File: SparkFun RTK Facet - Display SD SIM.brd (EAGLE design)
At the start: 50 x 22 mm, 32 parts, among them J1 QWIIC_RIGHT_ANGLE, J16 microSD

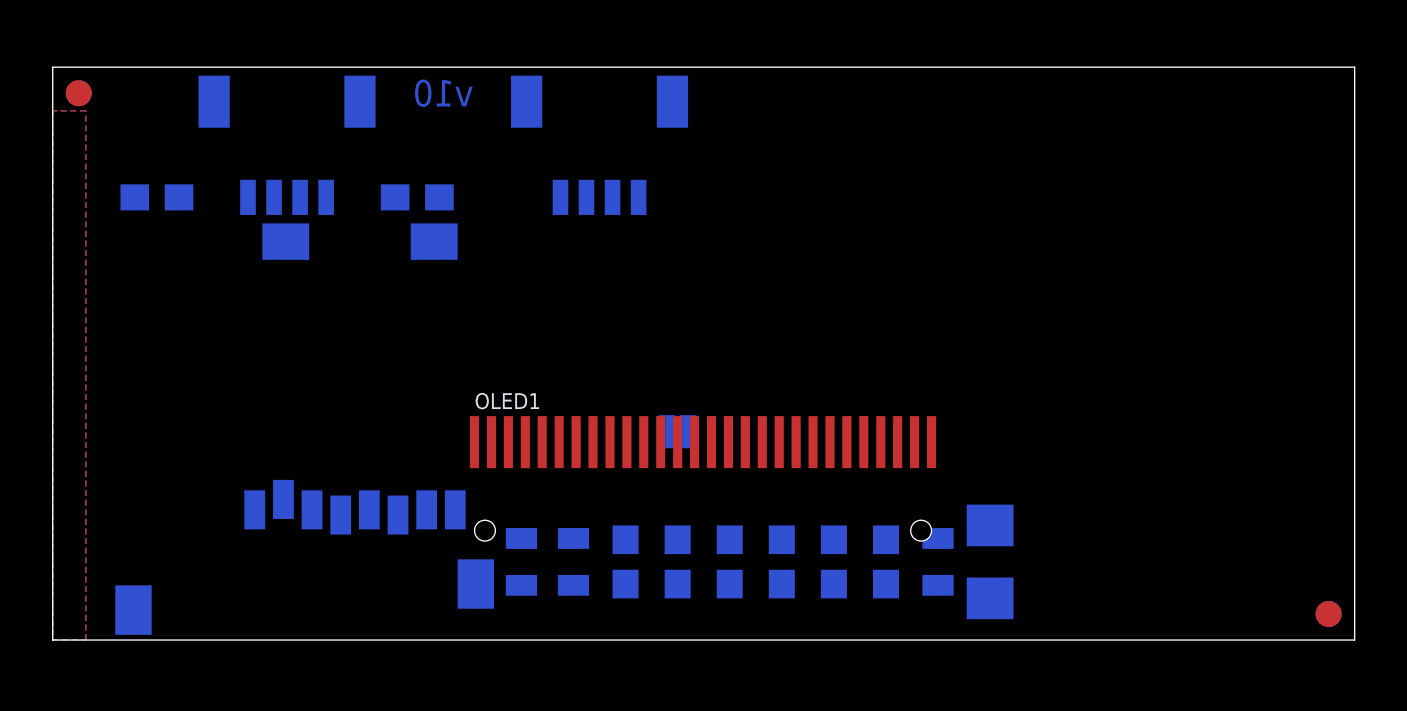
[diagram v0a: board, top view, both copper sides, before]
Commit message: Add 22ohm to USB hub D+/D-.
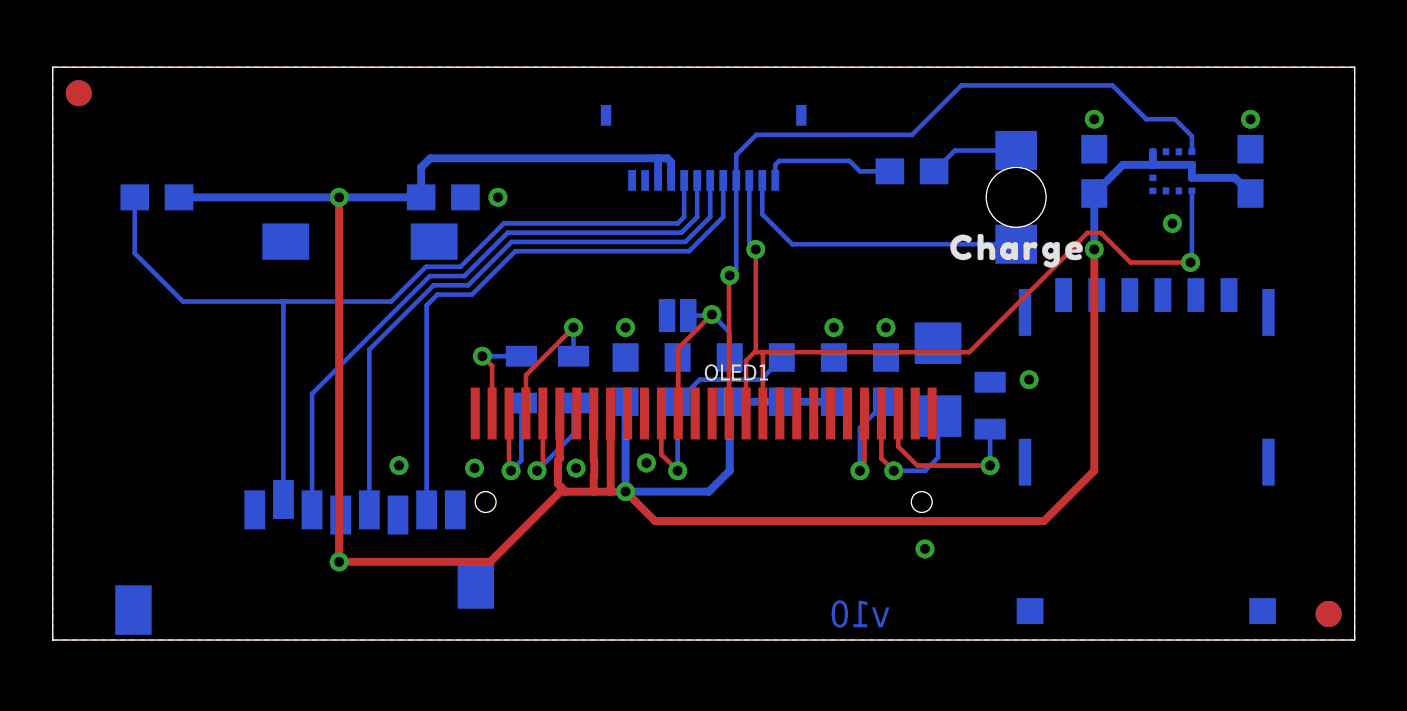
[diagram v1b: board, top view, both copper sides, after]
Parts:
- removed J2: (no value), SparkFun-Connectors:JST04_1MM_RA
- removed LOGO1: QWIIC_LOGO_CONNECTOR, SparkFun-Aesthetics:QWIIC_5.5MM
- removed U$2: (no value), output:ADDON3
- added C28: 0.1uF, SparkFun-Capacitors:0603
- added C8: 10uF, SparkFun-Capacitors:0603
- added D1: Green, SparkFun-LED:LED-1206-BOTTOM
- added J17: NANO_SIM, ublox:NANO_SIM_WURTH_693043020611
- added R5: 1k, SparkFun-Resistors:0603
- added U$8: (no value), output:CHARGE0
- added U13: LIS2DH12, SparkFun-Sensors:LGA-12-LISDH12
- J1: value QWIIC_RIGHT_ANGLE -> FPC_12_0.5MM2; device SparkFun-Connectors:JST04_1MM_RA -> RTK Facet:FPC_12_FLIP_DOUBLESIDED_2
- U$1: device output:SPI0 -> output:SD#DIS0
- moved FRAME1 104.1 mm to (-2.57, -29.5)
- moved U$1 20.6 mm to (25.0, 16.0), turned to 0 degrees
- moved U$4 20.1 mm to (28.0, 2.00)
- moved U$3 19.9 mm to (23.8, 2.00)
- moved U$5 19.7 mm to (19.5, 2.00)
- moved LOGO5 18.9 mm to (27.0, 5.00)
- moved U$6 18.8 mm to (25.1, 3.50)
- moved LOGO3 10.0 mm to (35.0, 2.00)
- moved OLED1 8.87 mm to (25.0, 8.70)
- moved C5 7.28 mm to (34.0, 10.0), turned to 90 degrees
- moved C7 7.28 mm to (24.0, 10.0), turned to 90 degrees
- moved R3 7.28 mm to (26.0, 10.0), turned to 270 degrees
- moved C2 7.00 mm to (20.0, 10.0), turned to 270 degrees
- moved C3 7.00 mm to (18.0, 10.0), turned to 270 degrees
- moved C4 7.00 mm to (30.0, 10.0), turned to 90 degrees
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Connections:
- removed net SCL: J1.4, OLED1.16
- removed net SDA: J1.3, OLED1.17, OLED1.18
- new net CHARGE_LED: D1.C, J1.11
- new net ESP_21/SDA: J1.10, OLED1.17, OLED1.18, U13.4
- new net ESP_22/SCL: J1.9, OLED1.16, U13.1
- new net N$3: D1.A, R5.1
- new net VIN: J1.12, R5.2
- net 3.3V: now also C28.1, C8.1, J1.3, J1.4, U13.10, U13.2, U13.3, U13.9; no longer J1.2
- net GND: now also C28.2, C8.2, J1.2, U13.5, U13.6, U13.7, U13.8
- net SD_!CS!: now also J1.5; no longer J2.1
- net SD_CIPO: now also J1.8; no longer J2.4
- net SD_COPI: now also J1.6; no longer J2.2
- net SD_SCK: now also J1.7; no longer J2.3
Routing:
- net 3.3V: track 0.00 -> 111.0 mm, vias 0 -> 4
- net SD_!CS!: track 0.00 -> 34.4 mm
- net ESP_21/SDA: track 0.00 -> 33.5 mm, vias 0 -> 2
- net ESP_22/SCL: track 0.00 -> 30.1 mm, vias 0 -> 1
- net SD_COPI: track 0.00 -> 23.5 mm
- net SD_SCK: track 0.00 -> 22.8 mm
- net SD_CIPO: track 0.00 -> 22.1 mm
- net CHARGE_LED: track 0.00 -> 11.5 mm
- net RESET: track 0.00 -> 9.84 mm, vias 0 -> 1
- net D/C: track 0.00 -> 7.19 mm, vias 0 -> 1
- net VCC: track 0.00 -> 6.50 mm, vias 0 -> 1
- net VCOMH: track 0.00 -> 5.90 mm, vias 0 -> 1
- net N$2: track 0.00 -> 5.47 mm, vias 0 -> 1
- net IREF: track 0.00 -> 5.34 mm, vias 0 -> 1
- net VIN: track 0.00 -> 5.23 mm
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
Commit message: Fix errors on all 3 boards after enclosure review.
* Flip connector board completely. Mirror connectors.
* Mirror connector on SD board
* Move LED above SIM socket
* Add membrane connector to SD board
* Remove switch connector from main board
* Increase width of connector board, 2mm on each side - 54mm wide
* Move LiPo Connector north as much as possible
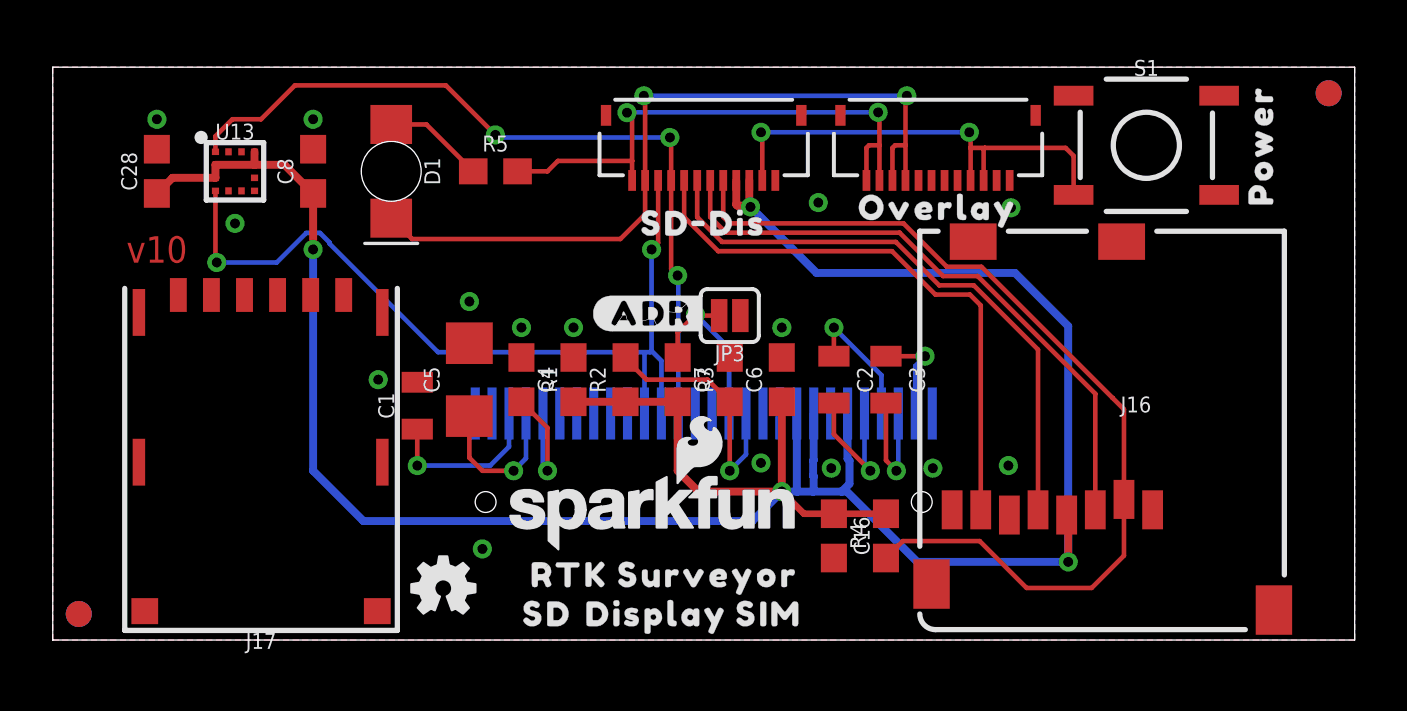
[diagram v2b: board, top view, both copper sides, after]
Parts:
- added J2: FPC_12_0.5MM2, RTK Facet:FPC_12_FLIP_DOUBLESIDED_2
- added S1: (no value), SparkFun-Switches:TACTILE_SWITCH_SMD_5.2MM
- added U$2: (no value), output:OVERLAY0
- added U$9: (no value), output:POWER0
- LOGO3: value OSHW-LOGOS -> OSHW-LOGOMINI; device SparkFun-Aesthetics:OSHW-LOGO-S -> SparkFun-Aesthetics:OSHW-LOGO-MINI
- moved FRAME1 55.1 mm to (52.6, -29.5), flipped to the bottom
- moved FID1 48.0 mm to (1.00, 1.00), flipped to the bottom
- moved FID2 48.0 mm to (49.0, 21.0), flipped to the bottom
- moved FID3 48.0 mm to (49.0, 21.0), flipped to the top
- moved FID4 48.0 mm to (1.00, 1.00), flipped to the top
- moved C28 42.0 mm to (4.00, 18.0), flipped to the top
- moved U13 36.0 mm to (7.00, 18.0), flipped to the top
- moved J17 34.0 mm to (8.00, 7.00), flipped to the top
- moved R4 30.9 mm to (32.0, 4.00), flipped to the top, turned to 90 degrees
- moved C8 30.0 mm to (10.0, 18.0), flipped to the top
- moved U$8 24.1 mm to (13.0, 16.0), flipped to the bottom
- moved D1 24.0 mm to (13.0, 18.0), flipped to the top
- moved C1 22.0 mm to (14.0, 9.00), flipped to the top
- moved LOGO3 20.0 mm to (15.0, 2.00), flipped to the top
- moved C16 19.8 mm to (30.0, 4.00), flipped to the top, turned to 270 degrees
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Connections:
- new net POWER_BTN: J1.2, J2.3, J2.4, S1.3
- net CHARGE_LED: now also J2.10, J2.9
- net GND: now also J2.1, J2.2, S1.1; no longer J1.2
- net VIN: now also J2.11, J2.12
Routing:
- net CHARGE_LED: track 11.5 -> 30.2 mm, vias 0 -> 2
- net POWER_BTN: track 0.00 -> 18.6 mm, vias 0 -> 2
- net VIN: track 5.23 -> 21.3 mm, vias 0 -> 2
- net 3.3V: track 111.0 -> 105.2 mm
- net SD_!CS!: track 34.4 -> 36.1 mm
- net ESP_22/SCL: track 30.1 -> 30.4 mm, vias 1 -> 3
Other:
- board text added: "FPC stiffener is 3mm"
